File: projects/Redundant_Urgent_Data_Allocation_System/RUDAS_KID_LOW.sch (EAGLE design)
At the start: 30 parts, among them IC1 5M240ZT100, IC2 STM32F103VGT6

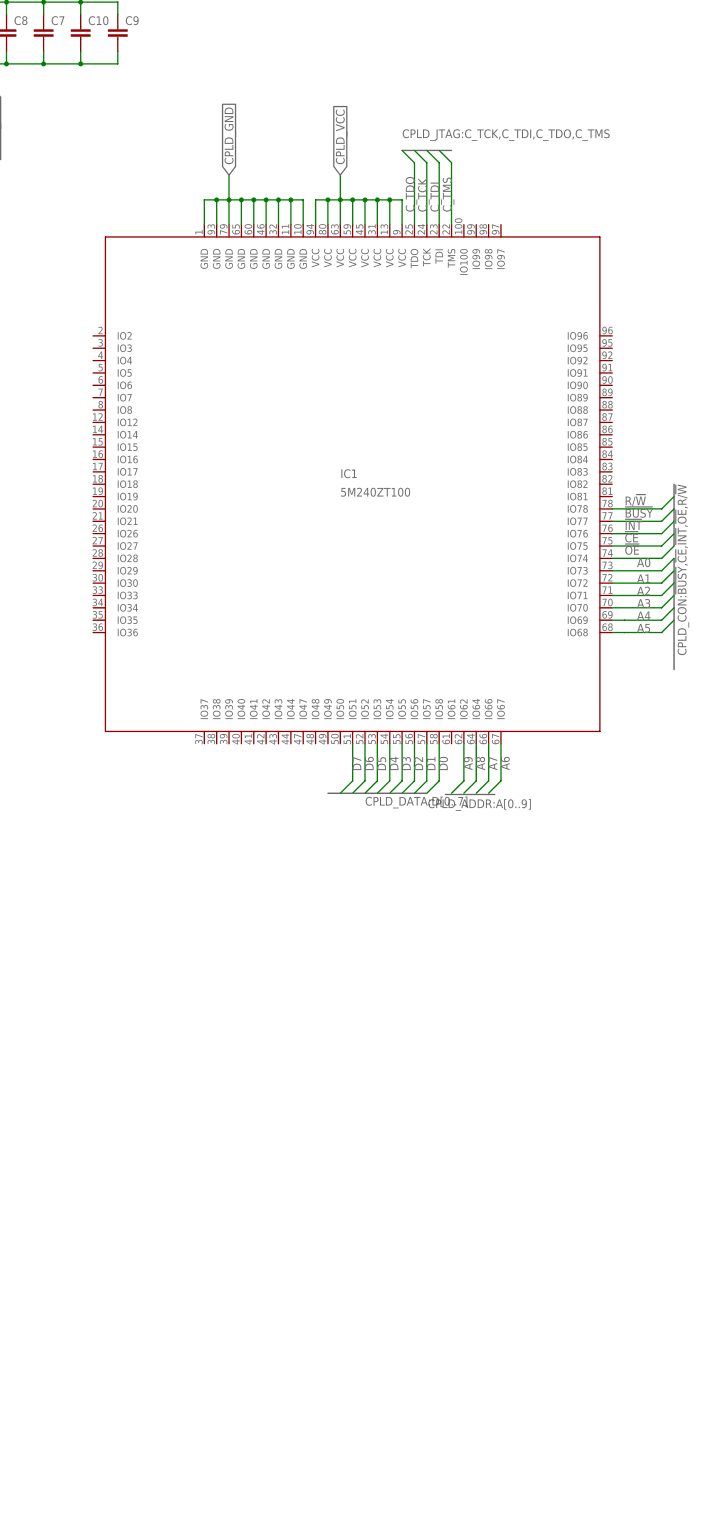
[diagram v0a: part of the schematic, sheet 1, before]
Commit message: add connector
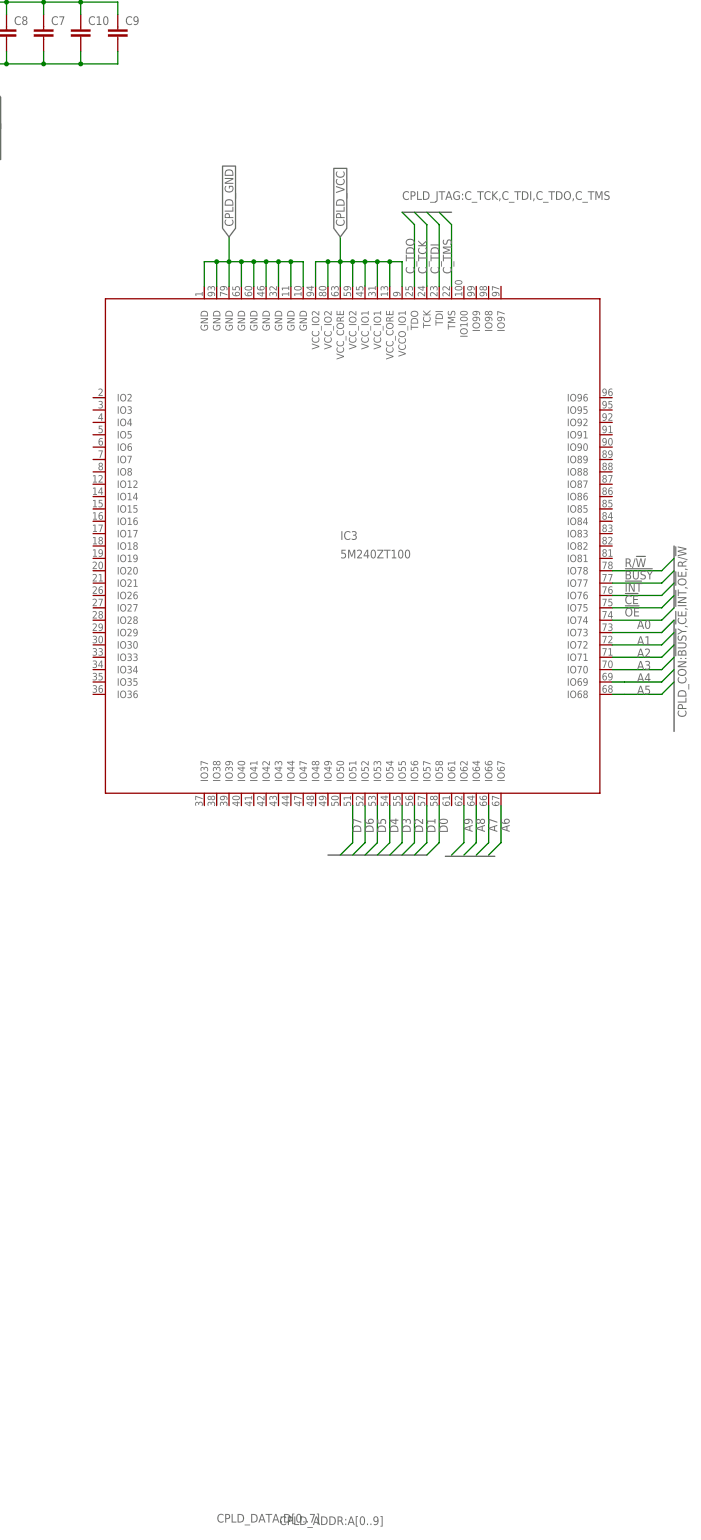
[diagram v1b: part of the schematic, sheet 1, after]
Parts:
- removed IC1: 5M240ZT100, ORBiT-IC-CPLD-Intel-MAX_V:5M240ZT100
- added IC3: 5M240ZT100, ORBiT-IC-CPLD-Intel-MAX_V:5M240ZT100
- C1, C10, C11, C12, C13, C14, C15, C16, C17, C18, C2, C3, C4, C5, C6, C7, C8, C9: device rcl:C-EUC0805 -> rcl:C-EUC2012
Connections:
- net !BUSY!: now also IC3.IO77; no longer IC1.IO77
- net !CE!: now also IC3.IO75; no longer IC1.IO75
- net !INT!: now also IC3.IO76; no longer IC1.IO76
- net !OE!: now also IC3.IO74; no longer IC1.IO74
- net A0: now also IC3.IO73; no longer IC1.IO73
- net A1: now also IC3.IO72; no longer IC1.IO72
- net A2: now also IC3.IO71; no longer IC1.IO71
- net A3: now also IC3.IO70; no longer IC1.IO70
- net A4: now also IC3.IO69; no longer IC1.IO69
- net A5: now also IC3.IO68; no longer IC1.IO68
- net A6: now also IC3.IO67; no longer IC1.IO67
- net A7: now also IC3.IO66; no longer IC1.IO66
- net A8: now also IC3.IO64; no longer IC1.IO64
- net A9: now also IC3.IO62; no longer IC1.IO62
- net CPLD_GND: now also IC3.GND@1, IC3.GND@2, IC3.GND@3, IC3.GND@4, IC3.GND@5, IC3.GND@6, IC3.GND@7, IC3.GND@8, IC3.GND@9; no longer IC1.GND@1, IC1.GND@2, IC1.GND@3, IC1.GND@4, IC1.GND@5, IC1.GND@6, IC1.GND@7, IC1.GND@8, IC1.GND@9
- net CPLD_VCC: now also IC3.VCCO_IO1@1, IC3.VCC_CORE@1, IC3.VCC_CORE@2, IC3.VCC_IO1@3, IC3.VCC_IO1@4, IC3.VCC_IO2@5, IC3.VCC_IO2@7, IC3.VCC_IO2@8; no longer IC1.VCC@1, IC1.VCC@2, IC1.VCC@3, IC1.VCC@4, IC1.VCC@5, IC1.VCC@6, IC1.VCC@7, IC1.VCC@8
- net C_TCK: now also IC3.TCK; no longer IC1.TCK
- net C_TDI: now also IC3.TDI; no longer IC1.TDI
- net C_TDO: now also IC3.TDO; no longer IC1.TDO
- net C_TMS: now also IC3.TMS; no longer IC1.TMS
- net D0: now also IC3.IO58; no longer IC1.IO58
- net D1: now also IC3.IO57; no longer IC1.IO57
- net D2: now also IC3.IO56; no longer IC1.IO56
- net D3: now also IC3.IO55; no longer IC1.IO55
- net D4: now also IC3.IO54; no longer IC1.IO54
- net D5: now also IC3.IO53; no longer IC1.IO53
- net D6: now also IC3.IO52; no longer IC1.IO52
- net D7: now also IC3.IO51; no longer IC1.IO51
- net R/!W!: now also IC3.IO78; no longer IC1.IO78

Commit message: add new part list
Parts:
- removed CAN_GND, CAN_H, CAN_L, CAN_VCC, UART_GND, UART_RX, UART_TX, UART_VCC: TP, ORBiT-special:TP
- added R1, R2, R3, R4, R5, R6, R7, R8, R9: (no value), rcl:R-EU_R2012
- added TP1, TP10, TP11, TP12, TP2, TP3, TP4, TP5, TP6, TP7, TP8, TP9: TP063, ORBiT-special:TP063
- added U$3: CONN-10PINR/A-10PIN, ORBIT-CONN HEADER-3M-2500 Series:CONN-10PINR/A-10PIN
- added U$4: CONN-20PINR/A-20PIN, ORBIT-CONN HEADER-3M-2500 Series:CONN-20PINR/A-20PIN
- added U$5: CARD_EDGE_50PINM80-5305042, ORBIT-CON-HARWIN-101LOK:CARD_EDGE_50PINM80-5305042
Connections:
- new net +12V: U$5.PIN1
- new net +3V: U$5.PIN3
- new net +5V: U$5.PIN27
- new net 12V_GND: U$5.PIN26
- new net 3V_GND: U$5.PIN28
- new net 5V_GND: U$5.PIN2
- new net CAN_H_P: U$2.CAN_H, U$5.PIN4
- new net CAN_H_S: U$5.PIN29
- new net CAN_L_P: U$2.CAN_L, U$5.PIN5
- new net CAN_L_S: U$5.PIN30
- new net CPLD_IO_VCC: R6.2, R7.2, R8.2, U$3.PIN7, U$3.PIN8
- new net CPLD_VCC_CORE: IC3.VCC_CORE@1, IC3.VCC_CORE@2
- new net CPLD_VCC_IO2: IC3.VCC_IO2@5, IC3.VCC_IO2@7, IC3.VCC_IO2@8
- new net CPL_VCC_IO1: IC3.VCCO_IO1@1, IC3.VCC_IO1@3, IC3.VCC_IO1@4
- new net LAN_CLK_N0: IC3.IO81, U$5.PIN9
- new net LAN_CLK_N1: IC3.IO85, U$5.PIN15
- new net LAN_CLK_N2: IC3.IO96, U$5.PIN21
- new net LAN_CLK_N3: IC3.IO29, U$5.PIN34
- new net LAN_CLK_N4: IC3.IO19, U$5.PIN40
- new net LAN_CLK_N5: IC3.IO5, U$5.PIN46
- new net LAN_CLK_P0: IC3.IO82, U$5.PIN10
- new net LAN_CLK_P1: IC3.IO86, U$5.PIN16
- new net LAN_CLK_P2: IC3.IO97, U$5.PIN22
- new net LAN_CLK_P3: IC3.IO28, U$5.PIN35
- new net LAN_CLK_P4: IC3.IO18, U$5.PIN41
- new net LAN_CLK_P5: IC3.IO4, U$5.PIN47
- new net LAN_N0: IC3.IO83, U$5.PIN11
- new net LAN_N1: IC3.IO87, U$5.PIN17
- new net LAN_N2: IC3.IO98, U$5.PIN23
- new net LAN_N3: IC3.IO27, U$5.PIN36
- new net LAN_N4: IC3.IO17, U$5.PIN42
- new net LAN_N5: IC3.IO3, U$5.PIN48
- new net LAN_P0: IC3.IO84, U$5.PIN12
- new net LAN_P1: IC3.IO88, U$5.PIN18
- new net LAN_P2: IC3.IO99, U$5.PIN24
- new net LAN_P3: IC3.IO26, U$5.PIN37
- new net LAN_P4: IC3.IO16, U$5.PIN43
- new net LAN_P5: IC3.IO2, U$5.PIN49
- new net NOTE0: U$5.PIN13
- new net NOTE1: U$5.PIN19
- new net NOTE2: U$5.PIN25
- new net NOTE3: U$5.PIN38
- new net NOTE4: U$5.PIN44
- new net NOTE5: U$5.PIN50
- new net SIGNAL_GND: U$2.GND2, U$5.PIN14, U$5.PIN20, U$5.PIN33, U$5.PIN39, U$5.PIN45, U$5.PIN8
- new net SIGNAL_VCC: U$2.VCC2
- net CPLD_GND: now also R9.1, U$3.PIN10, U$3.PIN6
- net CPLD_VCC: no longer IC3.VCCO_IO1@1, IC3.VCC_CORE@1, IC3.VCC_CORE@2, IC3.VCC_IO1@3, IC3.VCC_IO1@4, IC3.VCC_IO2@5, IC3.VCC_IO2@7, IC3.VCC_IO2@8
- net C_TCK: now also R9.2, U$3.PIN1
- net C_TDI: now also R8.1, U$3.PIN5
- net C_TDO: now also R6.1, U$3.PIN2
- net C_TMS: now also R7.1, U$3.PIN3
- net STM32_CAN_RX: now also TP7.TP
- net STM32_CAN_TX: now also TP8.TP
- net STM32_I2C1_SCL: now also TP9.TP
- net STM32_I2C1_SDA: now also TP10.TP
- net STM32_SPI1_CS: now also TP1.TP
- net STM32_SPI1_MISO: now also TP3.TP
- net STM32_SPI1_MOSI: now also TP4.TP
- net STM32_SPI1_SCK: now also TP2.TP
- net STM32_UART1_RX: now also TP6.TP; no longer UART_RX.TP
- net STM32_UART1_TX: now also TP5.TP; no longer UART_TX.TP
- net STM32_UART2_RX: now also TP12.TP
- net STM32_UART2_TX: now also TP11.TP
- net S_GND: now also R5.1, U$2.GND1, U$4.PIN12, U$4.PIN13, U$4.PIN14, U$4.PIN15, U$4.PIN16, U$4.PIN17, U$4.PIN18, U$4.PIN19, U$4.PIN20
- net S_RST: now also U$4.PIN9
- net S_TCK: now also R5.2, U$4.PIN5
- net S_TDI: now also R2.1, U$4.PIN3
- net S_TDO: now also R4.1, U$4.PIN7
- net S_TMS: now also R3.1, U$4.PIN4
- net S_TRST: now also R1.1, U$4.PIN2
- net S_VCC: now also R1.2, R2.2, R3.2, R4.2, U$2.VCC1, U$4.PIN1, U$4.PIN11

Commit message: add
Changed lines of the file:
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@@
 <attribute name="VALUE" x="-56.896" y="137.541" size="1.778" layer="96"/>
 </instance>
-<instance part="U$2" gate="G$1" x="-419.1" y="-7.62" smashed="yes"/>
+<instance part="U$2" gate="G$1" x="-421.64" y="-55.88" smashed="yes"/>
 <instance part="IC3" gate="G$1" x="60.96" y="35.56" smashed="yes">
 <attribute name="NAME" x="58.42" y="36.83" size="1.778" layer="95"/>
@@
 <segment>
 <pinref part="U$2" gate="G$1" pin="GND1"/>
-<wire x1="-424.18" y1="-29.972" x2="-424.18" y2="-35.56" width="0.1524" layer="91"/>
-<wire x1="-424.18" y1="-35.56" x2="-429.26" y2="-35.56" width="0.1524" layer="91"/>
-<label x="-429.26" y="-35.56" size="1.778" layer="95" rot="R180" xref="yes"/>
+<wire x1="-426.72" y1="-78.232" x2="-426.72" y2="-83.82" width="0.1524" layer="91"/>
+<wire x1="-426.72" y1="-83.82" x2="-431.8" y2="-83.82" width="0.1524" layer="91"/>
+<label x="-431.8" y="-83.82" size="1.778" layer="95" rot="R180" xref="yes"/>
 </segment>
 </net>
@@
 <segment>
 <pinref part="U$2" gate="G$1" pin="VCC1"/>
-<wire x1="-424.18" y1="10.668" x2="-424.18" y2="17.78" width="0.1524" layer="91"/>
-<wire x1="-424.18" y1="17.78" x2="-429.26" y2="17.78" width="0.1524" layer="91"/>
-<label x="-429.26" y="17.78" size="1.778" layer="95" rot="R180" xref="yes"/>
+<wire x1="-426.72" y1="-37.592" x2="-426.72" y2="-30.48" width="0.1524" layer="91"/>
+<wire x1="-426.72" y1="-30.48" x2="-431.8" y2="-30.48" width="0.1524" layer="91"/>
+<label x="-431.8" y="-30.48" size="1.778" layer="95" rot="R180" xref="yes"/>
 </segment>
 </net>
@@
 </segment>
 <segment>
-<wire x1="-436.88" y1="-10.16" x2="-457.2" y2="-10.16" width="0.1524" layer="91"/>
-<label x="-457.2" y="-7.62" size="1.778" layer="95" rot="MR180"/>
+<wire x1="-439.42" y1="-58.42" x2="-459.74" y2="-58.42" width="0.1524" layer="91"/>
+<label x="-459.74" y="-55.88" size="1.778" layer="95" rot="MR180"/>
 <pinref part="U$2" gate="G$1" pin="RX"/>
-<wire x1="-434.34" y1="-12.192" x2="-436.88" y2="-12.192" width="0.1524" layer="91"/>
-<wire x1="-436.88" y1="-12.192" x2="-436.88" y2="-10.16" width="0.1524" layer="91"/>
+<wire x1="-436.88" y1="-60.452" x2="-439.42" y2="-60.452" width="0.1524" layer="91"/>
+<wire x1="-439.42" y1="-60.452" x2="-439.42" y2="-58.42" width="0.1524" layer="91"/>
 </segment>
 <segment>
@@
 </segment>
 <segment>
-<wire x1="-449.58" y1="-5.08" x2="-457.2" y2="-5.08" width="0.1524" layer="91"/>
-<label x="-457.2" y="-2.54" size="1.778" layer="95" rot="MR180"/>
+<wire x1="-452.12" y1="-53.34" x2="-459.74" y2="-53.34" width="0.1524" layer="91"/>
+<label x="-459.74" y="-50.8" size="1.778" layer="95" rot="MR180"/>
 <pinref part="U$2" gate="G$1" pin="TX"/>
-<wire x1="-434.34" y1="-7.112" x2="-436.88" y2="-7.112" width="0.1524" layer="91"/>
-<wire x1="-436.88" y1="-7.112" x2="-436.88" y2="-5.08" width="0.1524" layer="91"/>
-<wire x1="-436.88" y1="-5.08" x2="-449.58" y2="-5.08" width="0.1524" layer="91"/>
+<wire x1="-436.88" y1="-55.372" x2="-439.42" y2="-55.372" width="0.1524" layer="91"/>
+<wire x1="-439.42" y1="-55.372" x2="-439.42" y2="-53.34" width="0.1524" layer="91"/>
+<wire x1="-439.42" y1="-53.34" x2="-452.12" y2="-53.34" width="0.1524" layer="91"/>
 </segment>
 <segment>
@@
 </segment>
 <segment>
-<wire x1="-401.32" y1="-12.192" x2="-396.24" y2="-12.192" width="0.1524" layer="91"/>
+<wire x1="-403.86" y1="-60.452" x2="-398.78" y2="-60.452" width="0.1524" layer="91"/>
 <pinref part="U$2" gate="G$1" pin="CAN_L"/>
-<label x="-396.24" y="-12.7" size="1.778" layer="95"/>
+<label x="-398.78" y="-60.96" size="1.778" layer="95"/>
 </segment>
 </net>
@@
 <segment>
 <pinref part="U$2" gate="G$1" pin="CAN_H"/>
-<wire x1="-401.32" y1="-7.112" x2="-396.24" y2="-7.112" width="0.1524" layer="91"/>
-<label x="-396.24" y="-7.62" size="1.778" layer="95"/>
+<wire x1="-403.86" y1="-55.372" x2="-398.78" y2="-55.372" width="0.1524" layer="91"/>
+<label x="-398.78" y="-55.88" size="1.778" layer="95"/>
 </segment>
 </net>
@@
 <segment>
 <pinref part="U$2" gate="G$1" pin="GND2"/>
-<wire x1="-408.94" y1="-29.972" x2="-408.94" y2="-35.56" width="0.1524" layer="91"/>
-<wire x1="-408.94" y1="-35.56" x2="-406.4" y2="-35.56" width="0.1524" layer="91"/>
-<label x="-406.4" y="-35.56" size="1.778" layer="95" xref="yes"/>
+<wire x1="-411.48" y1="-78.232" x2="-411.48" y2="-83.82" width="0.1524" layer="91"/>
+<wire x1="-411.48" y1="-83.82" x2="-408.94" y2="-83.82" width="0.1524" layer="91"/>
+<label x="-408.94" y="-83.82" size="1.778" layer="95" xref="yes"/>
 </segment>
 </net>
@@
 <segment>
 <pinref part="U$2" gate="G$1" pin="VCC2"/>
-<wire x1="-408.94" y1="10.668" x2="-408.94" y2="17.78" width="0.1524" layer="91"/>
-<wire x1="-408.94" y1="17.78" x2="-406.4" y2="17.78" width="0.1524" layer="91"/>
-<label x="-406.4" y="17.78" size="1.778" layer="95" xref="yes"/>
-</segment>
-</net>
+<wire x1="-411.48" y1="-37.592" x2="-411.48" y2="-30.48" width="0.1524" layer="91"/>
+<wire x1="-411.48" y1="-30.48" x2="-408.94" y2="-30.48" width="0.1524" layer="91"/>
+<label x="-408.94" y="-30.48" size="1.778" layer="95" xref="yes"/>
+</segment>
+</net>
